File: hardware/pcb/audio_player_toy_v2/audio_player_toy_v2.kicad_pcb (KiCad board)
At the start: 2 copper layers, 40 x 55 mm, 13 parts, among them J1 Conn_02x05_Odd_Even, J2 TYPE-C-31-M-12, U1 ISD2360YYI

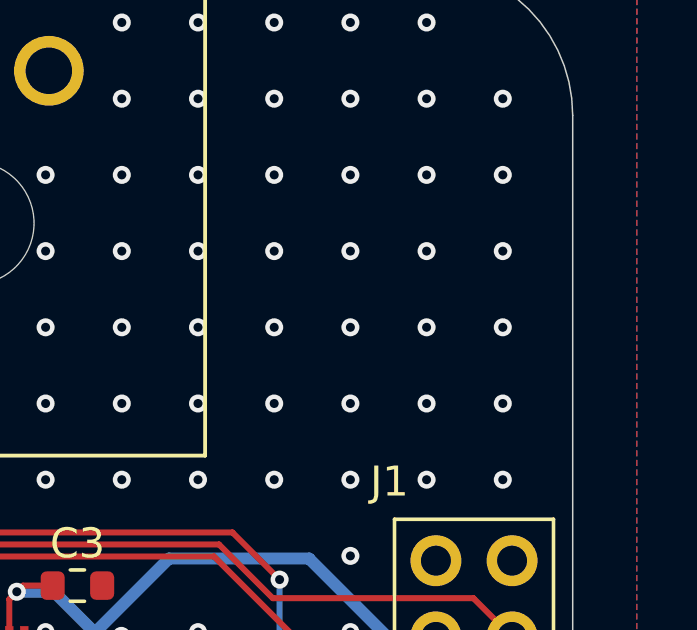
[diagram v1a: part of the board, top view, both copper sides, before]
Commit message: chore: add label on v1 and v2
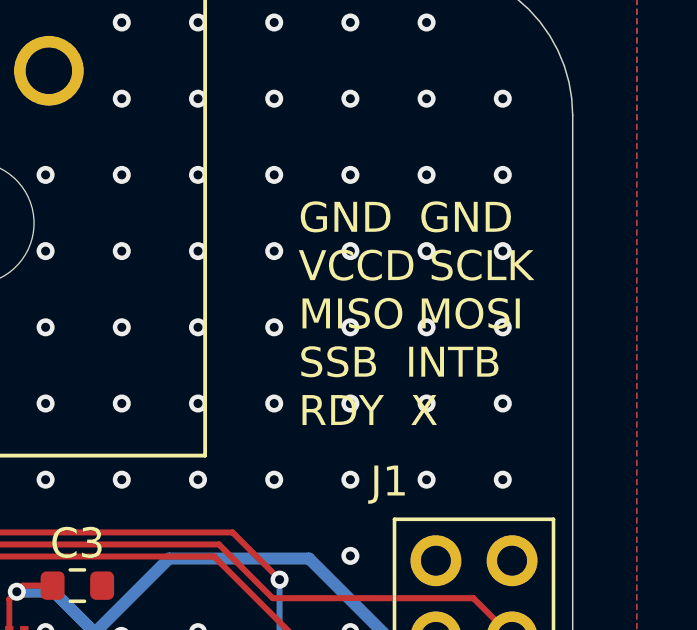
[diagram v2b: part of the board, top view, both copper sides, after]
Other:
- board text added: "GND GND VCCD SCLK MISO MOSI SSB INTB RDY X"
